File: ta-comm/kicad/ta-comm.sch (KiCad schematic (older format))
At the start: 52 parts

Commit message: Initial communication board PCB
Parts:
- added J3: Conn_01x04, ta-comm:MountingHoles_TartanArtibeus, symbol Connector_Generic:Conn_01x04
- C1, C13, C14, C17, C18, C20, C4, C7, C8, C9: renamed from C?; footprint CAPC1608X90N -> ta-comm:CAPC1608X90N
- C10, C11, C12, C15, C16, C19, C2, C3, C5, C6: renamed from C?; footprint CAPC1608X87N -> ta-comm:CAPC1608X87N
- FB1: renamed from FB?; footprint BEADC1608X95N -> ta-comm:BEADC1608X95N
- IC1: renamed from IC?; footprint QFN50P200X200X55-13N-D -> ta-comm:QFN50P200X200X55-13N-D
- IC2: renamed from IC?; footprint (none) -> ta-comm:STA0693A
- IC3: renamed from IC?; footprint RFFM6404 -> ta-comm:RFFM6404
- IC4: renamed from IC?; footprint QFN50P600X600X100-37N-D -> ta-comm:QFN50P600X600X100-37N-D
- J1: renamed from J?; footprint A1JB -> ta-comm:A1JB
- J2: renamed from J?; footprint (none) -> ta-comm:PinSocket_1x4_TartanArtibeus
- J4, J5: renamed from J?; footprint (none) -> ta-comm:PinSocket_1x16_TartanArtibeus
- L1, L2: renamed from L?; footprint INDC1608X100N -> ta-comm:INDC1608X100N
- LED1, LED2: renamed from LED?; footprint LGQ396PS35 -> ta-comm:LGQ396PS35
- R1, R10, R11, R12, R13, R14, R15, R16, R17, R18, R2, R3, R4, R5, R6, R7, R8, R9: renamed from R?; footprint RESC1608X55N -> ta-comm:RESC1608X55N
- Y1: renamed from Y?; footprint FOX924B27 -> ta-comm:FOX924B27
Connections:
- net D0: now also J5.4 (Pin_4)
- net GND: now also J3.1 (Pin_1), J3.2 (Pin_2), J3.3 (Pin_3), J3.4 (Pin_4)
- no-connect marks 29 -> 28

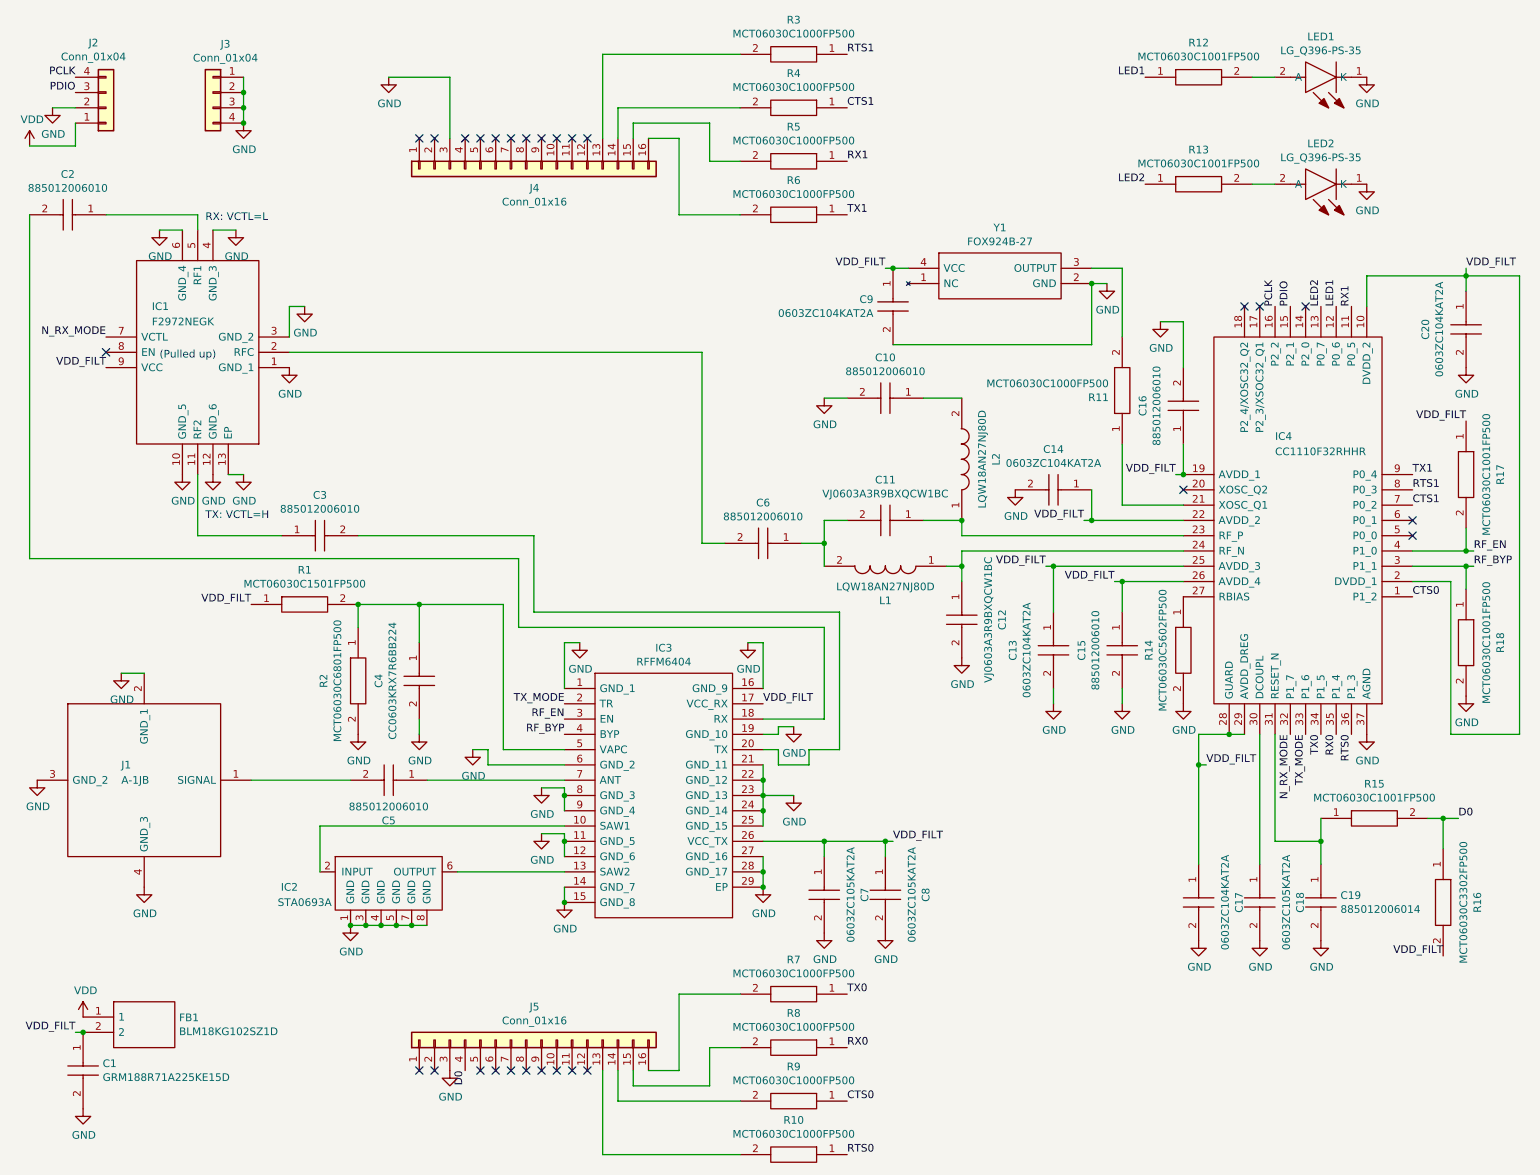
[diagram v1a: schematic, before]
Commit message: Updates communication board schematic
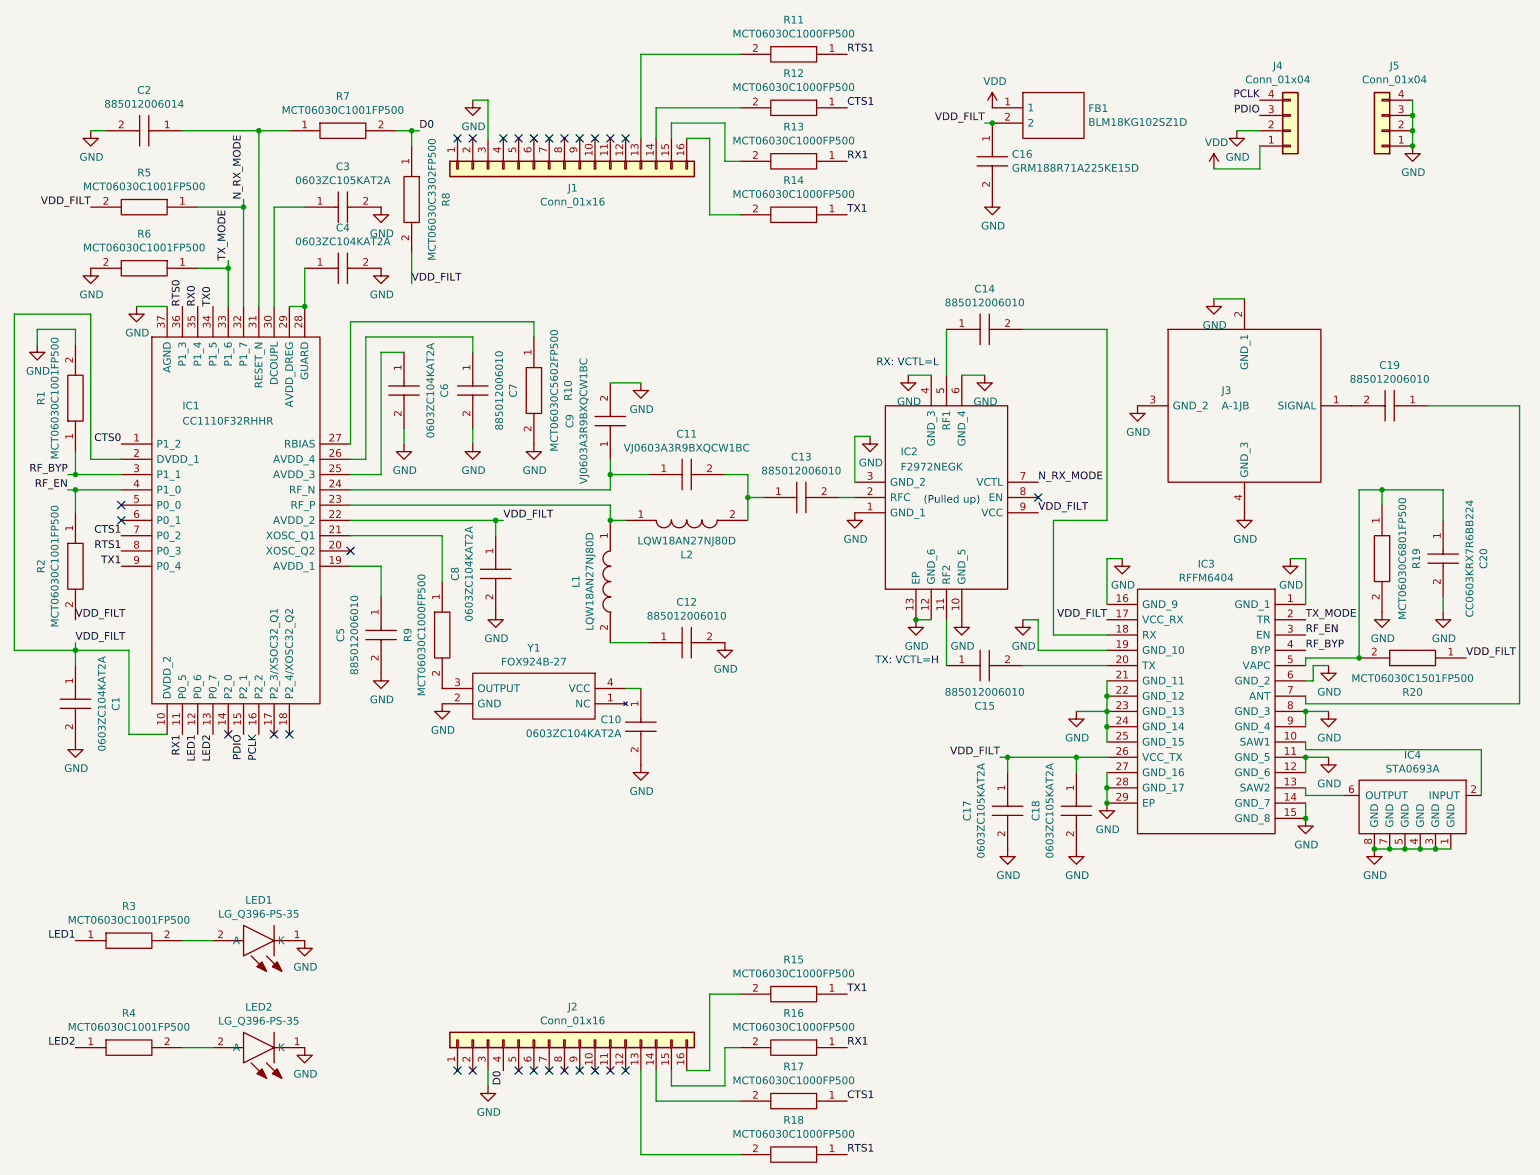
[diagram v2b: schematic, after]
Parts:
- removed C1: GRM188R71A225KE15D, ta-comm:CAPC1608X90N, symbol ta-comm:GRM188R71A225KE15D
- removed C10, C16, C2, C3, C6: 885012006010, ta-comm:CAPC1608X87N, symbol ta-comm:885012006010
- removed C12: VJ0603A3R9BXQCW1BC, ta-comm:CAPC1608X87N, symbol ta-comm:VJ0603A3R9BXQCW1BC
- removed C13, C14, C17, C20, C9: 0603ZC104KAT2A, ta-comm:CAPC1608X90N, symbol ta-comm:0603ZC104KAT2A
- removed C19: 885012006014, ta-comm:CAPC1608X87N, symbol ta-comm:885012006014
- removed C4: CC0603KRX7R6BB224, ta-comm:CAPC1608X90N, symbol ta-comm:CC0603KRX7R6BB224
- removed C7, C8: 0603ZC105KAT2A, ta-comm:CAPC1608X90N, symbol ta-comm:0603ZC105KAT2A
- removed IC1: F2972NEGK, ta-comm:QFN50P200X200X55-13N-D, symbol ta-comm:F2972NEGK
- removed IC2: STA0693A, ta-comm:STA0693A, symbol ta-comm:STA0693A
- removed IC4: CC1110F32RHHR, ta-comm:QFN50P600X600X100-37N-D, symbol ta-comm:CC1110F32RHHR
- removed J1: A-1JB, ta-comm:A1JB, symbol ta-comm:A-1JB
- removed J2: Conn_01x04, ta-comm:PinSocket_1x4_TartanArtibeus, symbol Connector_Generic:Conn_01x04
- removed J3: Conn_01x04, ta-comm:MountingHoles_TartanArtibeus, symbol Connector_Generic:Conn_01x04
- removed J4, J5: Conn_01x16, ta-comm:PinSocket_1x16_TartanArtibeus, symbol Connector_Generic:Conn_01x16
- removed R1: MCT06030C1501FP500, ta-comm:RESC1608X55N, symbol ta-comm:MCT06030C1501FP500
- removed R10, R3, R4, R5, R6, R7, R8: MCT06030C1000FP500, ta-comm:RESC1608X55N, symbol ta-comm:MCT06030C1000FP500
- removed R12, R13, R15, R17, R18: MCT06030C1001FP500, ta-comm:RESC1608X55N, symbol ta-comm:MCT06030C1001FP500
- removed R14: MCT06030C5602FP500, ta-comm:RESC1608X55N, symbol ta-comm:MCT06030C5602FP500
- removed R16: MCT06030C3302FP500, ta-comm:RESC1608X55N, symbol ta-comm:MCT06030C3302FP500
- removed R2: MCT06030C6801FP500, ta-comm:RESC1608X55N, symbol ta-comm:MCT06030C6801FP500
- added C1, C10, C4, C6, C8: 0603ZC104KAT2A, ta-comm:CAPC1608X90N, symbol ta-comm:0603ZC104KAT2A
- added C12, C13, C14, C19, C7: 885012006010, ta-comm:CAPC1608X87N, symbol ta-comm:885012006010
- added C16: GRM188R71A225KE15D, ta-comm:CAPC1608X90N, symbol ta-comm:GRM188R71A225KE15D
- added C17, C3: 0603ZC105KAT2A, ta-comm:CAPC1608X90N, symbol ta-comm:0603ZC105KAT2A
- added C2: 885012006014, ta-comm:CAPC1608X87N, symbol ta-comm:885012006014
- added C20: CC0603KRX7R6BB224, ta-comm:CAPC1608X90N, symbol ta-comm:CC0603KRX7R6BB224
- added C9: VJ0603A3R9BXQCW1BC, ta-comm:CAPC1608X87N, symbol ta-comm:VJ0603A3R9BXQCW1BC
- added IC1: CC1110F32RHHR, ta-comm:QFN50P600X600X100-37N-D, symbol ta-comm:CC1110F32RHHR
- added IC2: F2972NEGK, ta-comm:QFN50P200X200X55-13N-D, symbol ta-comm:F2972NEGK
- added IC4: STA0693A, ta-comm:STA0693A, symbol ta-comm:STA0693A
- added J1, J2: Conn_01x16, ta-comm:PinSocket_1x16_TartanArtibeus, symbol Connector_Generic:Conn_01x16
- added J3: A-1JB, ta-comm:A1JB, symbol ta-comm:A-1JB
- added J4: Conn_01x04, ta-comm:PinSocket_1x4_TartanArtibeus, symbol Connector_Generic:Conn_01x04
- added J5: Conn_01x04, ta-comm:MountingHoles_TartanArtibeus, symbol Connector_Generic:Conn_01x04
- added R1, R2, R3, R4, R5, R6, R7: MCT06030C1001FP500, ta-comm:RESC1608X55N, symbol ta-comm:MCT06030C1001FP500
- added R10: MCT06030C5602FP500, ta-comm:RESC1608X55N, symbol ta-comm:MCT06030C5602FP500
- added R12, R13, R14, R15, R16, R17, R18: MCT06030C1000FP500, ta-comm:RESC1608X55N, symbol ta-comm:MCT06030C1000FP500
- added R19: MCT06030C6801FP500, ta-comm:RESC1608X55N, symbol ta-comm:MCT06030C6801FP500
- added R20: MCT06030C1501FP500, ta-comm:RESC1608X55N, symbol ta-comm:MCT06030C1501FP500
- added R8: MCT06030C3302FP500, ta-comm:RESC1608X55N, symbol ta-comm:MCT06030C3302FP500
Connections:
- net CTS0: now also IC1.1 (P1_2); no longer R9.1
- net CTS1: now also IC1.7 (P0_2), R12.1, R17.1
- net D0: now also J2.4 (Pin_4), R7.2, R8.1
- net GND: now also C5.2, C1.2, C10.2, C12.2, C16.2, C17.2, C2.2, C20.2, C3.2, C4.2, C6.2, C7.2, C8.2, C9.2, IC1.37 (AGND), IC2.1 (GND_1), IC2.10 (GND_5), IC2.12 (GND_6), IC2.13 (EP), IC2.3 (GND_2), IC2.4 (GND_3), IC2.6 (GND_4), IC4.1 (GND), IC4.3 (GND), IC4.4 (GND), IC4.5 (GND), IC4.7 (GND), IC4.8 (GND), J1.3 (Pin_3), J2.3 (Pin_3), J3.2 (GND_1), J3.3 (GND_2), J3.4 (GND_3), J4.2 (Pin_2), J5.1 (Pin_1), J5.2 (Pin_2), J5.3 (Pin_3), J5.4 (Pin_4), R1.2, R10.2, R19.2, R6.2; no longer C15.2
- net LED1: now also IC1.12 (P0_6), R3.1
- net LED2: now also IC1.13 (P0_7), R4.1
- net N_RX_MODE: now also IC1.32 (P1_7), IC2.7 (VCTL), R5.1
- net PCLK: now also IC1.16 (P2_2), J4.4 (Pin_4)
- net PDIO: now also IC1.15 (P2_1), J4.3 (Pin_3)
- net RF_BYP: now also IC1.3 (P1_1), R1.1
- net RF_EN: now also IC1.4 (P1_0), R2.1
- net RTS0: now also IC1.36 (P1_3)
- net RTS1: now also R11.1, IC1.8 (P0_3), R18.1
- net RX0: now also IC1.35 (P1_4)
- net RX1: now also IC1.11 (P0_5), R13.1, R16.1
- net TX0: now also IC1.34 (P1_5)
- net TX1: now also IC1.9 (P0_4), R14.1, R15.1
- net TX_MODE: now also IC1.33 (P1_6), R6.1
- net VDD: now also J4.1 (Pin_1)
- net VDD_FILT: now also C18.1, C1.1, C16.1, C17.1, C8.1, IC1.10 (DVDD_2), IC1.2 (DVDD_1), IC1.22 (AVDD_2), IC2.9 (VCC), R2.2, R20.1, R5.2, R8.2; no longer C15.1, Y1.4 (VCC)
- net at R9.2: now also Y1.3 (OUTPUT)
- net at R11.2: now also J1.13 (Pin_13); no longer Y1.3 (OUTPUT)
- net at L2.1: now also L1.1, IC1.23 (RF_P); no longer C11.1
- net at IC3.10 (SAW1): now also IC4.2 (INPUT)
- net at IC3.13 (SAW2): now also IC4.6 (OUTPUT)
- net at IC3.18 (RX): now also C14.2
- net at IC3.20 (TX): now also C15.2
- net at IC3.5 (VAPC): now also C20.1, R19.1, R20.2
- net at C5.1: now also IC1.19 (AVDD_1); no longer IC3.7 (ANT)
- net at LED2.2 (A): now also R4.2
- net at LED1.2 (A): now also R3.2
- net at L2.2: now also C11.2, C13.1
- net at L1.2: now also C12.1; no longer C11.2
- new net: IC1.21 (XOSC_Q1), R9.1
- new net: C11.1, C9.1, IC1.24 (RF_N)
- new net: C6.1, IC1.25 (AVDD_3)
- new net: C7.1, IC1.26 (AVDD_4)
- new net: IC1.27 (RBIAS), R10.1
- new net: C4.1, IC1.28 (GUARD), IC1.29 (AVDD_DREG)
- new net: C3.1, IC1.30 (DCOUPL)
- new net: C2.1, IC1.31 (RESET_N), R7.1
- new net: C10.1, Y1.4 (VCC)
- new net: C13.2, IC2.2 (RFC)
- new net: C15.1, IC2.11 (RF2)
- new net: C14.1, IC2.5 (RF1)
- new net: C19.1, IC3.7 (ANT)
- new net: J2.16 (Pin_16), R15.2
- new net: J2.15 (Pin_15), R16.2
- new net: J2.14 (Pin_14), R17.2
- new net: J2.13 (Pin_13), R18.2
- new net: J1.14 (Pin_14), R12.2
- new net: J1.15 (Pin_15), R13.2
- new net: J1.16 (Pin_16), R14.2
- new net: C19.2, J3.1 (SIGNAL)

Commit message: Updates communication board PCB
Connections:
- net CTS0: now also R12.1
- net CTS1: no longer R12.1
- net RTS0: now also R11.1
- net RTS1: no longer R11.1
- net RX0: now also R13.1
- net RX1: no longer R13.1
- net TX0: now also R14.1
- net TX1: no longer R14.1
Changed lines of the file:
@@
 $EndComp
 Text Label 6050 750  0    50   ~ 0
-RTS1
+RTS0
 Text Label 6050 1100 0    50   ~ 0
-CTS1
+CTS0
 Text Label 6050 1450 0    50   ~ 0
-RX1
+RX0
 Text Label 6050 1800 0    50   ~ 0
-TX1
+TX0
 Wire Wire Line
 	5350 1100 4800 1100
